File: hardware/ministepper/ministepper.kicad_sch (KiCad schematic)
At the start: 19 parts, among them J2 TC2030_NL, U1 STM32G0B1KBU6, U4 SIT3088EEUA

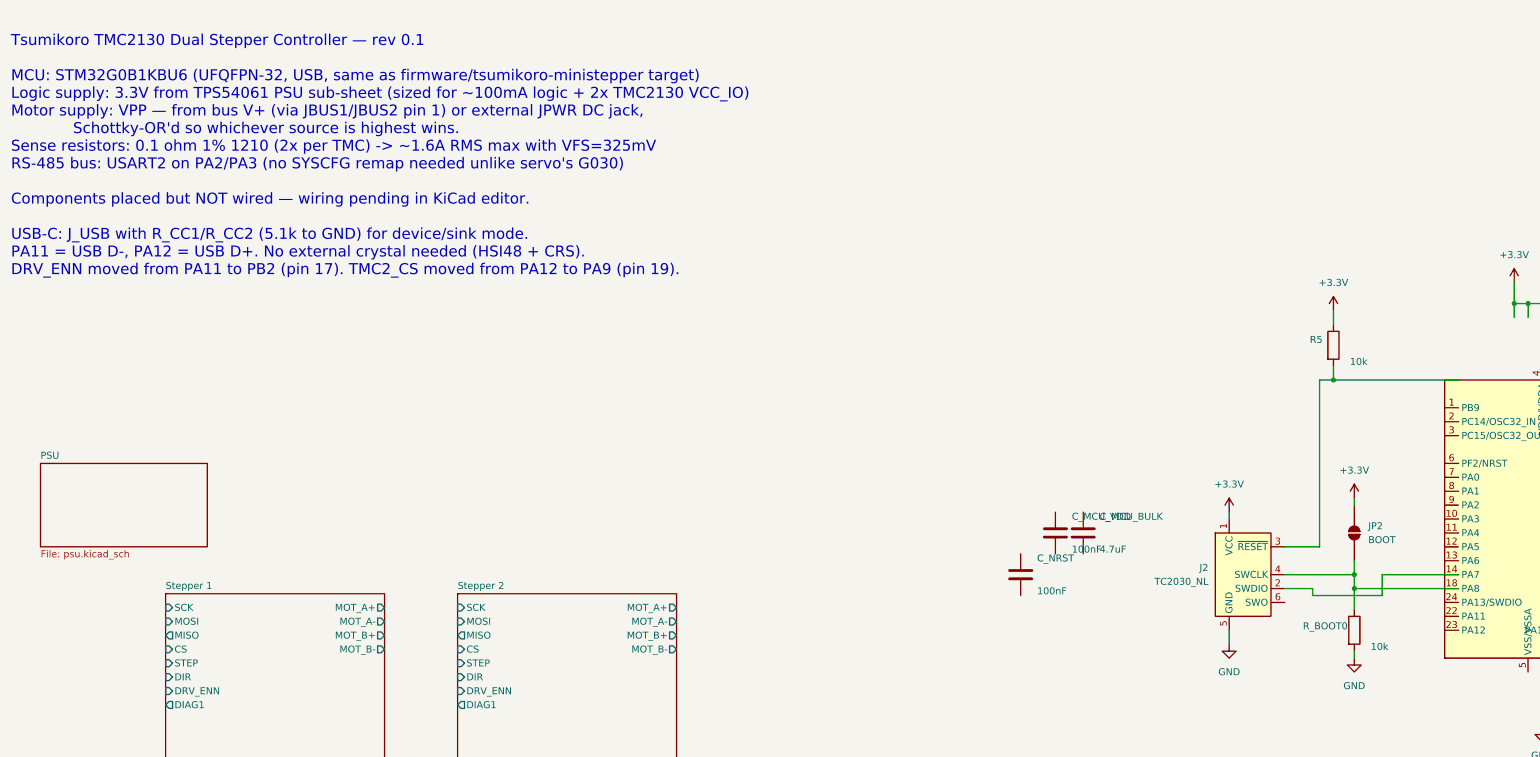
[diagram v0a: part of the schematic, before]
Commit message: hw/ministepper: add TS-1187A tactile BOOT button
SW_BOOT (XKB TS-1187A-B-A-B, C318884) connects PA14/BOOT0 to +3V3
when pressed. Hold during reset to enter the G0B1's system bootloader
(USART2, I2C1, SPI1, or USB DFU). Same part and footprint as the
bridge board's reset/boot buttons. TP_BOOT0 test pad retained as
pogo-pin fallback.

Co-Authored-By: Claude Opus 4.6 (1M context) <noreply@anthropic.com>
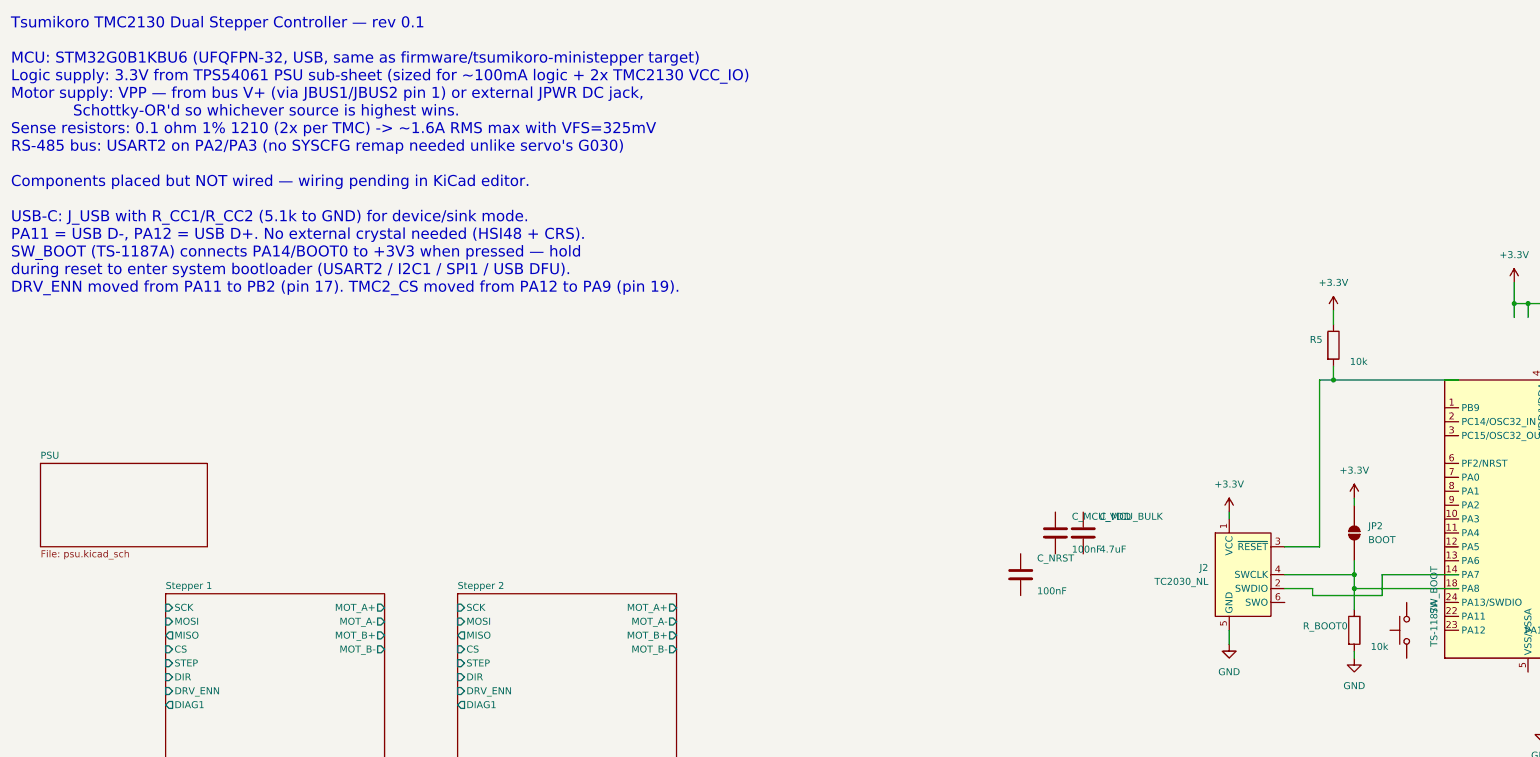
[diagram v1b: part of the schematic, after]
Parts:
- added SW_BOOT: TS-1187A, tsumikoro:SW_Push_1P1T_XKB_TS-1187A, symbol Switch:SW_Push
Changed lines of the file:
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@@
 		(comment 2 "Motor supply: bus V+ or external DC jack")
 	)
-	(text "Tsumikoro TMC2130 Dual Stepper Controller — rev 0.1\n\nMCU: STM32G0B1KBU6 (UFQFPN-32, USB, same as firmware/tsumikoro-ministepper target)\nLogic supply: 3.3V from TPS54061 PSU sub-sheet (sized for ~100mA logic + 2x TMC2130 VCC_IO)\nMotor supply: VPP — from bus V+ (via JBUS1/JBUS2 pin 1) or external JPWR DC jack,\n             Schottky-OR'd so whichever source is highest wins.\nSense resistors: 0.1 ohm 1% 1210 (2x per TMC) -> ~1.6A RMS max with VFS=325mV\nRS-485 bus: USART2 on PA2/PA3 (no SYSCFG remap needed unlike servo's G030)\n\nComponents placed but NOT wired — wiring pending in KiCad editor.\n\nUSB-C: J_USB with R_CC1/R_CC2 (5.1k to GND) for device/sink mode.\nPA11 = USB D-, PA12 = USB D+. No external crystal needed (HSI48 + CRS).\nDRV_ENN moved from PA11 to PB2 (pin 17). TMC2_CS moved from PA12 to PA9 (pin 19)."
+	(text "Tsumikoro TMC2130 Dual Stepper Controller — rev 0.1\n\nMCU: STM32G0B1KBU6 (UFQFPN-32, USB, same as firmware/tsumikoro-ministepper target)\nLogic supply: 3.3V from TPS54061 PSU sub-sheet (sized for ~100mA logic + 2x TMC2130 VCC_IO)\nMotor supply: VPP — from bus V+ (via JBUS1/JBUS2 pin 1) or external JPWR DC jack,\n             Schottky-OR'd so whichever source is highest wins.\nSense resistors: 0.1 ohm 1% 1210 (2x per TMC) -> ~1.6A RMS max with VFS=325mV\nRS-485 bus: USART2 on PA2/PA3 (no SYSCFG remap needed unlike servo's G030)\n\nComponents placed but NOT wired — wiring pending in KiCad editor.\n\nUSB-C: J_USB with R_CC1/R_CC2 (5.1k to GND) for device/sink mode.\nPA11 = USB D-, PA12 = USB D+. No external crystal needed (HSI48 + CRS).\nSW_BOOT (TS-1187A) connects PA14/BOOT0 to +3V3 when pressed — hold\nduring reset to enter system bootloader (USART2 / I2C1 / SPI1 / USB DFU).\nDRV_ENN moved from PA11 to PB2 (pin 17). TMC2_CS moved from PA12 to PA9 (pin 19)."
 		(exclude_from_sim no)
 		(at 20 20 0)
@@
 					(unit 1)
 				)
+			)
+		)
+	)
+	(symbol
+		(lib_id "Switch:SW_Push")
+		(at 275 106.68 90)
+		(unit 1)
+		(body_style 1)
+		(exclude_from_sim no)
+		(in_bom yes)
+		(on_board yes)
+		(in_pos_files yes)
+		(dnp no)
+		(property "Reference" "SW_BOOT"
+			(at 280 103.68 0)
+			(show_name no)
+			(do_not_autoplace no)
+			(effects
+				(font
+					(size 1.27 1.27)
+				)
+				(justify left)
+			)
+		)
+		(property "Value" "TS-1187A"
+			(at 280 109.68 0)
+			(show_name no)
+			(do_not_autoplace no)
+			(effects
+				(font
+					(size 1.27 1.27)
+				)
+				(justify left)
+			)
+		)
+		(property "Footprint" "tsumikoro:SW_Push_1P1T_XKB_TS-1187A"
+			(at 275 106.68 0)
+			(hide yes)
+			(show_name no)
+			(do_not_autoplace no)
+			(effects
+				(font
+					(size 1.27 1.27)
+				)
+			)
+		)
+		(property "Datasheet" ""
+			(at 275 106.68 0)
+			(hide yes)
+			(show_name no)
+			(do_not_autoplace no)
+			(effects
+				(font
+					(size 1.27 1.27)
+				)
+			)
+		)
+		(property "Description" "BOOT0 button: press during reset to enter system bootloader"
+			(at 275 106.68 0)
+			(hide yes)
+			(show_name no)
+			(do_not_autoplace no)
+			(effects
+				(font
+					(size 1.27 1.27)
+				)
+			)
+		)
+		(property "LCSC" "C318884"
+			(at 275 106.68 0)
+			(hide yes)
+			(show_name no)
+			(do_not_autoplace no)
+			(effects
+				(font
+					(size 1.27 1.27)
+				)
+			)
+		)
+		(property "MPN" "TS-1187A-B-A-B"
+			(at 275 106.68 0)
+			(hide yes)
+			(show_name no)
+			(do_not_autoplace no)
+			(effects
+				(font
+					(size 1.27 1.27)
+				)
+			)
+		)
+		(property "Manufacturer" "XKB"
+			(at 275 106.68 0)
+			(hide yes)
+			(show_name no)
+			(do_not_autoplace no)
+			(effects
+				(font
+					(size 1.27 1.27)
+				)
+			)
+		)
+		(pin "1"
+		)
+		(pin "2"
+		)
+		(instances
+			(project "ministepper"
+				(path "/e1d2c3b4-a5f6-7890-abcd-ef9876543210"
+					(reference "SW_BOOT")
+					(unit 1)
+				)

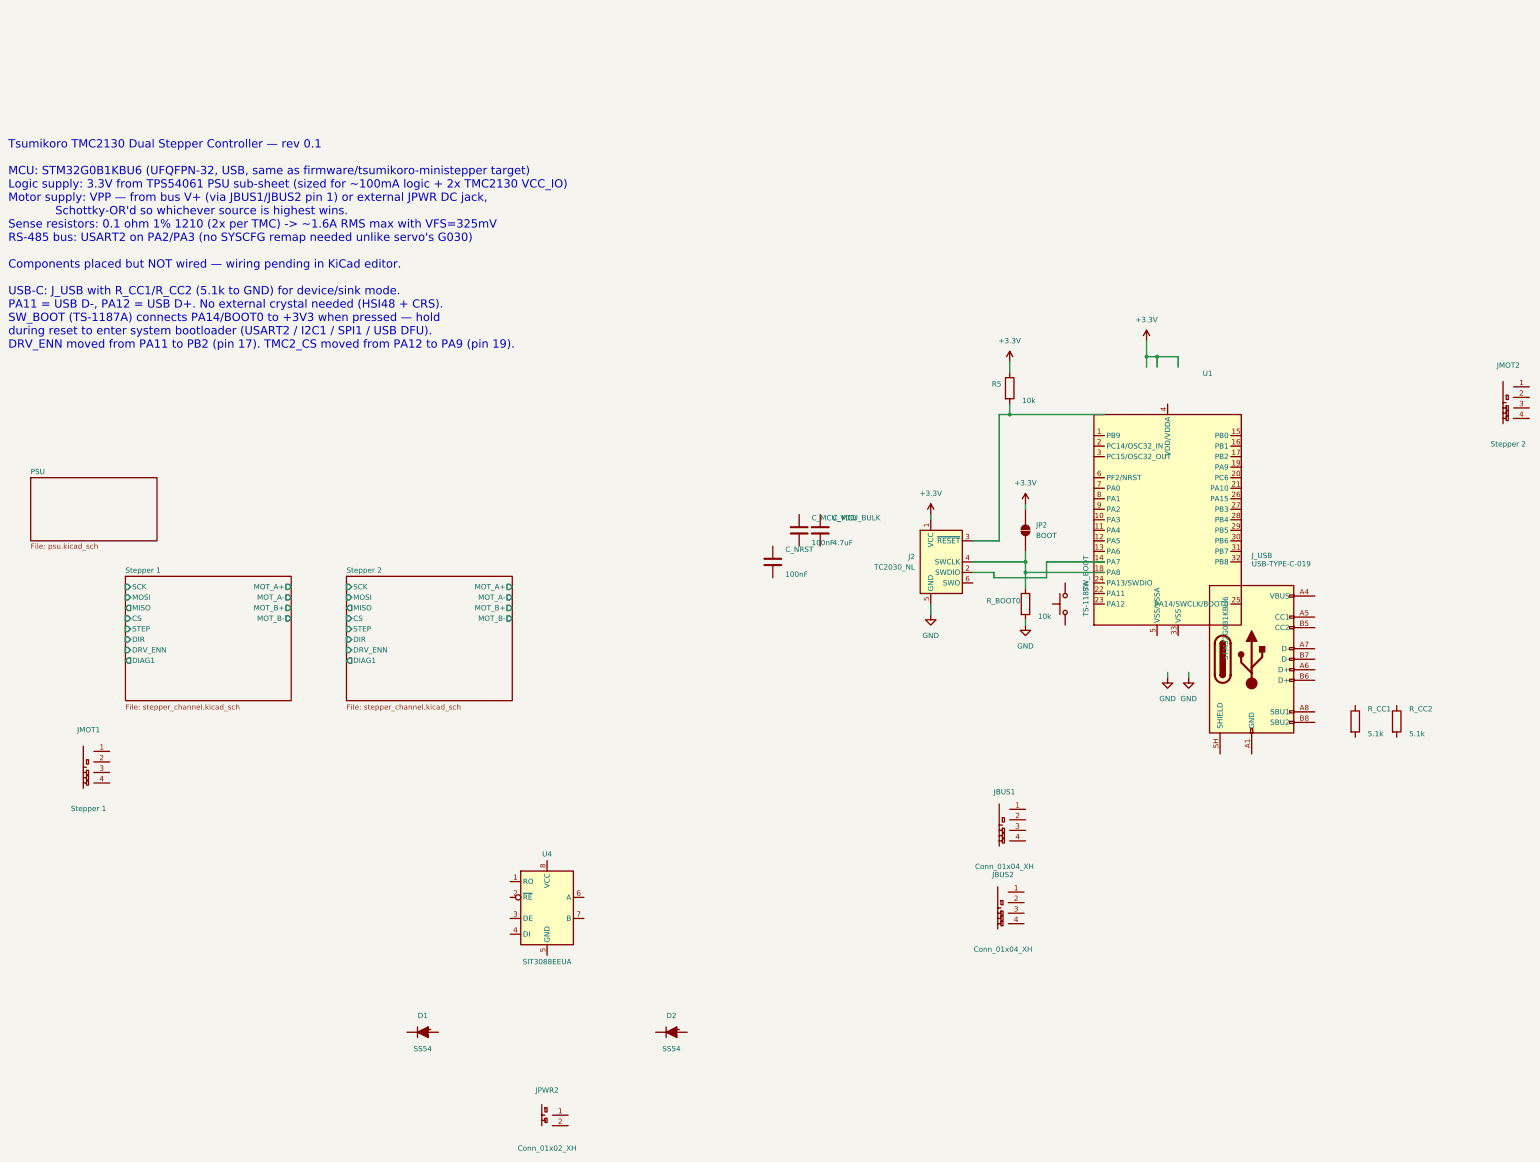
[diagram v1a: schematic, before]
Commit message: hw/ministepper: add full pinout table to schematic text note
Embeds the 32-pin G0B1 UFQFPN-32 target wiring table directly in the
root schematic sheet so the pin assignment is visible alongside the
components during wiring without needing to reference external docs.

Co-Authored-By: Claude Opus 4.6 (1M context) <noreply@anthropic.com>
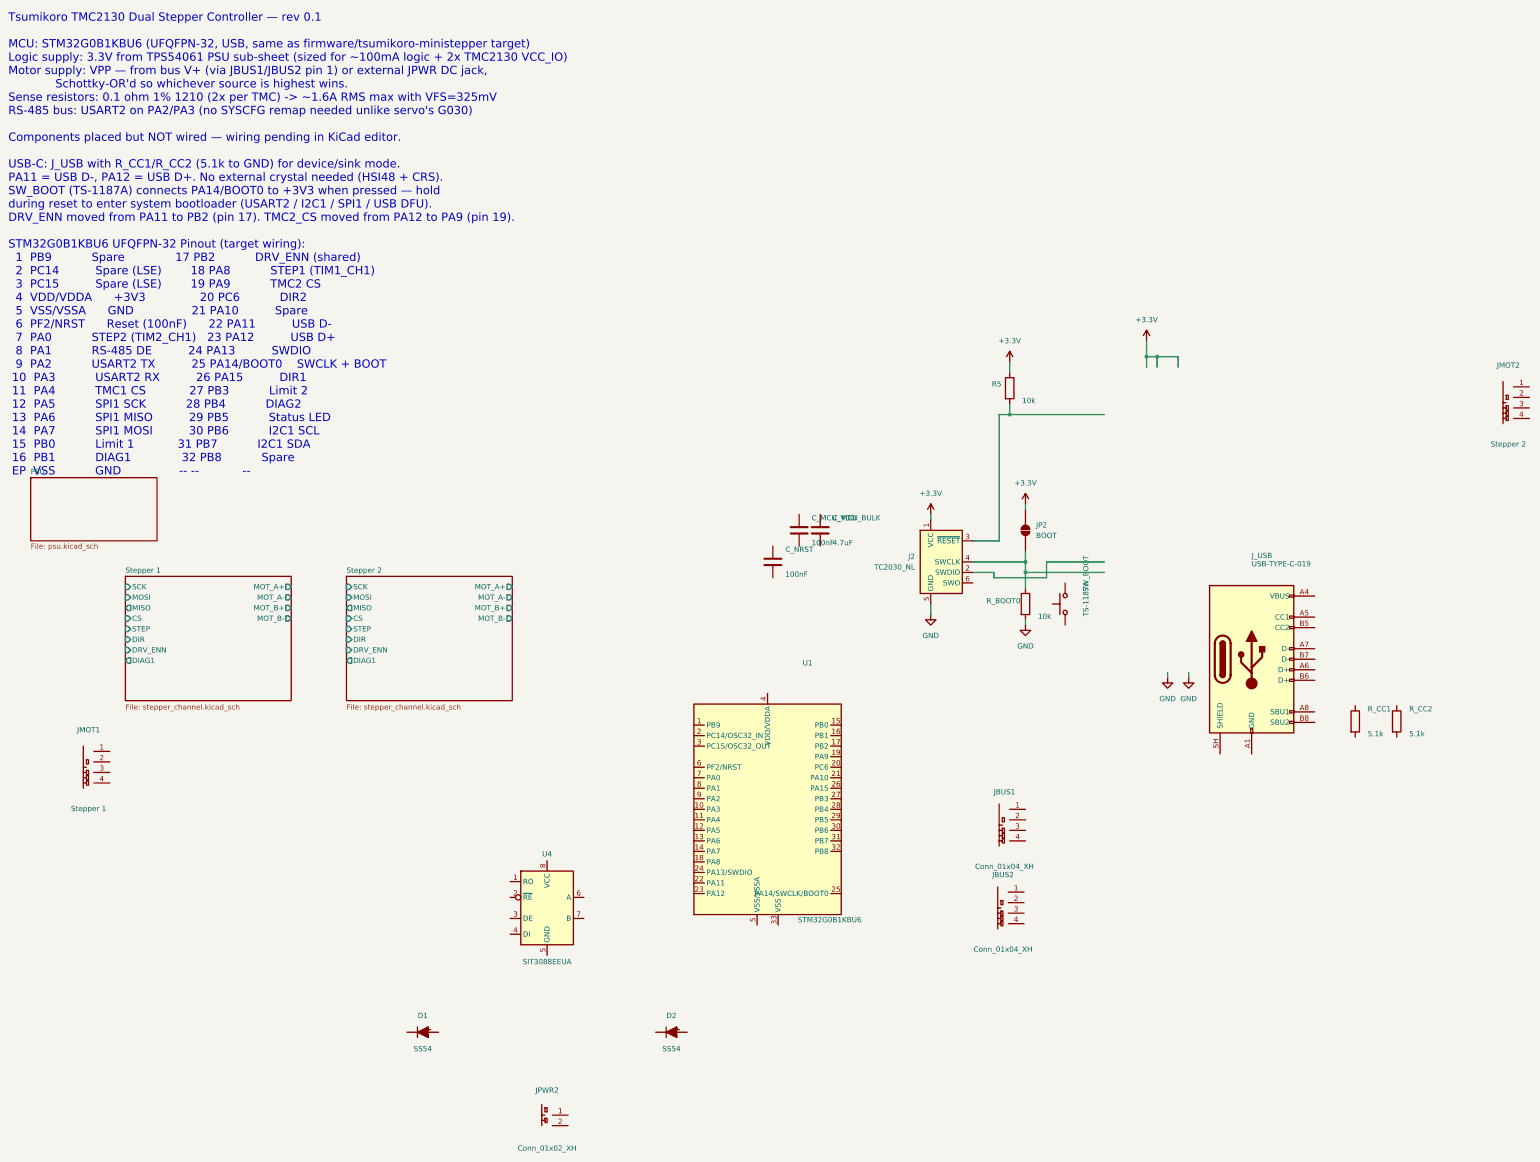
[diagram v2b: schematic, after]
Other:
- moved on the sheet: U1
